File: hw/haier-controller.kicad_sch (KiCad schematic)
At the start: 95 parts, among them J1 USB4105-GF-A, J10 DG240W, J11 DG240W, J12 DG240W, J2 10118194-0001LF, J3 TC2050-IDC-NL, J4 Goldpin, J5 BM04B, J6 S3B-XH-A-1, J7 S3B-XH-A-1, J8 S4B-XH-A-1, J9 S4B-XH-A-1, K1 HFD27-005-S, K2 HFD23/005-1ZS, K3 HFD23/005-1ZS, K4 HFD23/005-1ZS, Q1 MMBT3904, Q2 MMBT3904, Q3 MMBT3904, Q4 MMBT3904, Q5 MMBT3904, SW1 PTS526SM15SMTR2_LFS, U1 ESP32-C6, U2 LM66200DRLR, U3 LD1117S33CTR, U4 USBLC6-4SC6, U5 DS2401+, U6 MAX3485EESA+T

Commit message: Updated R1,R3,J3
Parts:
- J3: footprint (none) -> connectors:TC2050-IDC-NL
- R1, R3: footprint (none) -> SMD:C_0603
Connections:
- no-connect marks 15 -> 16
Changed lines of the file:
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@@
 	)
 	(no_connect
+		(at 182.88 106.68)
+	)
+	(no_connect
 		(at 259.08 121.92)
 	)
@@
 			)
 		)
-		(property "Footprint" ""
+		(property "Footprint" "SMD:C_0603"
 			(at 43.815 40.64 0)
 			(hide yes)
@@
 			)
 		)
-		(property "Footprint" ""
+		(property "Footprint" "SMD:C_0603"
 			(at 43.815 38.1 0)
 			(hide yes)
@@
 			)
 		)
-		(property "Footprint" ""
+		(property "Footprint" "connectors:TC2050-IDC-NL"
 			(at 26.67 137.795 0)
 			(hide yes)

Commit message: Update footprints, Import to PCB
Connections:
- no-connect marks 16 -> 18
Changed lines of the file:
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@@
 	)
 	(no_connect
+		(at 131.445 100.33)
+	)
+	(no_connect
 		(at 41.275 154.305)
 	)
@@
 	)
 	(no_connect
-		(at 182.88 106.68)
+		(at 131.445 102.87)
 	)
 	(no_connect
@@
 	)
 	(no_connect
+		(at 131.445 97.79)
+	)
+	(no_connect
 		(at 196.215 53.975)
 	)
@@
 		(pin "1"
 		)
+		(pin "4"
+		)
 		(instances

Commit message: Finish PCB
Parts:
- removed J3: TC2050-IDC-NL, connectors:TC2050-IDC-NL, symbol Connectors:TC2050-IDC-NL
- added H1, H2, H3, H4: M3, mechanical:M3-Hole, symbol Misc:M3-Mount
- added J3: FTSH-105-01-L-DV-K, connectors:FTSH-105-01-L-DV-K, symbol Connectors:FTSH-105-01-L-DV-K
- R1, R3: footprint SMD:C_0603 -> SMD:R_0603
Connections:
- net 1W_ID: now also U1.14 (IO13); no longer U1.9 (IO1)
- net COOL_SW: now also U1.17 (IO19); no longer U1.11 (IO10)
- net DS18B20: now also U1.13 (IO12); no longer U1.8 (IO0)
- net ESP_EN: now also J3.10 (RST)
- net ESP_TCK: now also J3.4 (TCK/SWDCLK)
- net ESP_TDI: now also U4.4 (I/O3), J3.8 (TDI); no longer U4.6 (I/O4)
- net ESP_TDO: now also U4.6 (I/O4), J3.6 (TDO/SWO); no longer U4.4 (I/O3)
- net ESP_TMS: now also J3.2 (TMS/SWDIO)
- net HEAT_SW: now also U1.18 (IO20); no longer U1.26 (IO3)
- net LIM_SW: now also U1.16 (IO18); no longer U1.12 (IO11)
- net RS_SWITCH: now also U1.12 (IO11); no longer U1.27 (IO2)
- net VBUS: now also C6.2, C7.2, C8.2, D10.1, D11.1, D12.1, D9.1, K1.8 (GND), K2.5 (GND), K3.5 (GND), K4.5 (GND), R2.1, R20.2, R21.2, R22.2, R23.2, TP3.1, U2.2 (VOUT), U2.7 (VOUT), U3.3 (VIN); no longer C1.2, C2.2, J1.A4 (VBUS), J1.A9 (VBUS), TP2.1
- net GND: now reaches Q5.3 (E)
- net GND: now also C1.1, C10.1, C11.1, C12.1, C13.1, C14.1, C15.1, C16.2, C2.1, C3.1, C4.1, C5.1, C6.1, C7.1, C8.1, C9.1, D1.1, D2.1, D3.1, D4.1, D5.1, D6.2, D8.1, J1.A1 (GND), J1.A12 (GND), J1.SH (Shield), J2.5 (GND), J2.SH, J4.2, J5.4, J5.SH, J6.2, J7.2, Q1.3 (E), Q2.3 (E), Q3.3 (E), Q4.3 (E), R1.1, R12.2, R13.2, R3.1, SW1.2, TP6.1, U1.1 (GND), U1.28 (GND), U1.29 (EPAD), U2.1 (GND), U2.4 (~{ON}), U2.5 (GND), U3.1 (GND), U4.2 (GND), U5.1 (GND), U6.5 (GND), H1.1, H2.1, H3.1, H4.1, J3.3 (GND), J3.5 (GND), J3.7 (VDD), J3.9 (GND)
- net +3.3V: now reaches C16.1, U6.8 (VCC)
- net +3.3V: now also C10.2, C11.2, C12.2, C15.2, C9.2, J5.1, J6.3, J7.3, R11.1, R14.1, R4.1, R6.2, R7.1, R8.1, TP4.1, U1.2 (3V3), U3.2 (VOUT), U4.5 (VBUS), J3.1 (VREF)
- net at K4.3 (COM1), K4.4 (COM1): now also J12.2; no longer J12.1
- net at K4.6 (NO1): now also J12.1; no longer J12.2
- net at K2.3 (COM1), K2.4 (COM1): now also J10.2; no longer J10.1
- net at K2.6 (NO1): now also J10.1; no longer J10.2
- net VBUS_B: now reaches C3.2, J2.1 (VCC), TP1.1
- net VBUS_B: now also C4.2, U2.3 (VIN1)
- net VBUS_A: now reaches C5.2, U2.6 (VIN2)
- net VBUS_A: now also C1.2, C2.2, J1.A4 (VBUS), J1.A9 (VBUS), TP2.1
- net at K3.3 (COM1), K3.4 (COM1): now also J11.2; no longer J11.1
- net at K3.6 (NO1): now also J11.1; no longer J11.2
- net at R9.1: now also U1.11 (IO10); no longer U1.16 (IO18)
- no-connect marks 18 -> 19
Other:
- moved on the sheet: J10, J11, J12, J4

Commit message: Clean ERC errors
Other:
- moved on the sheet: C1, C10, C11, C12, C14, C15, C16, C2, C3, C4, C5, C6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

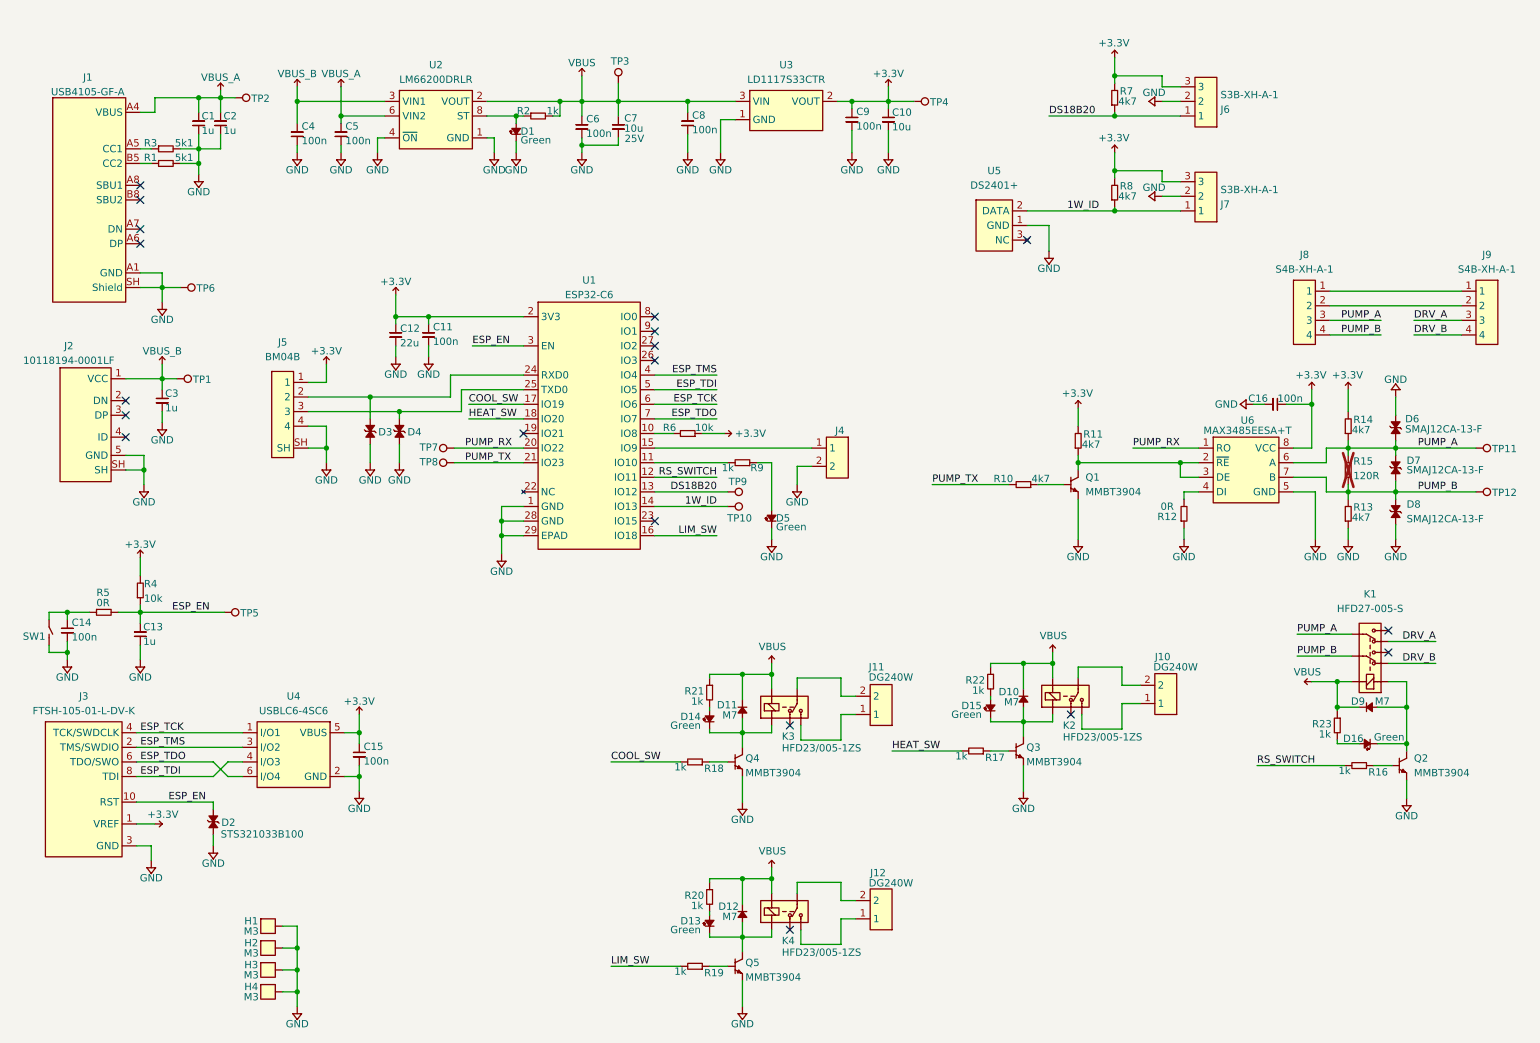
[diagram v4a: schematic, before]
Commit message: Update components, Add silkscreen descriptors
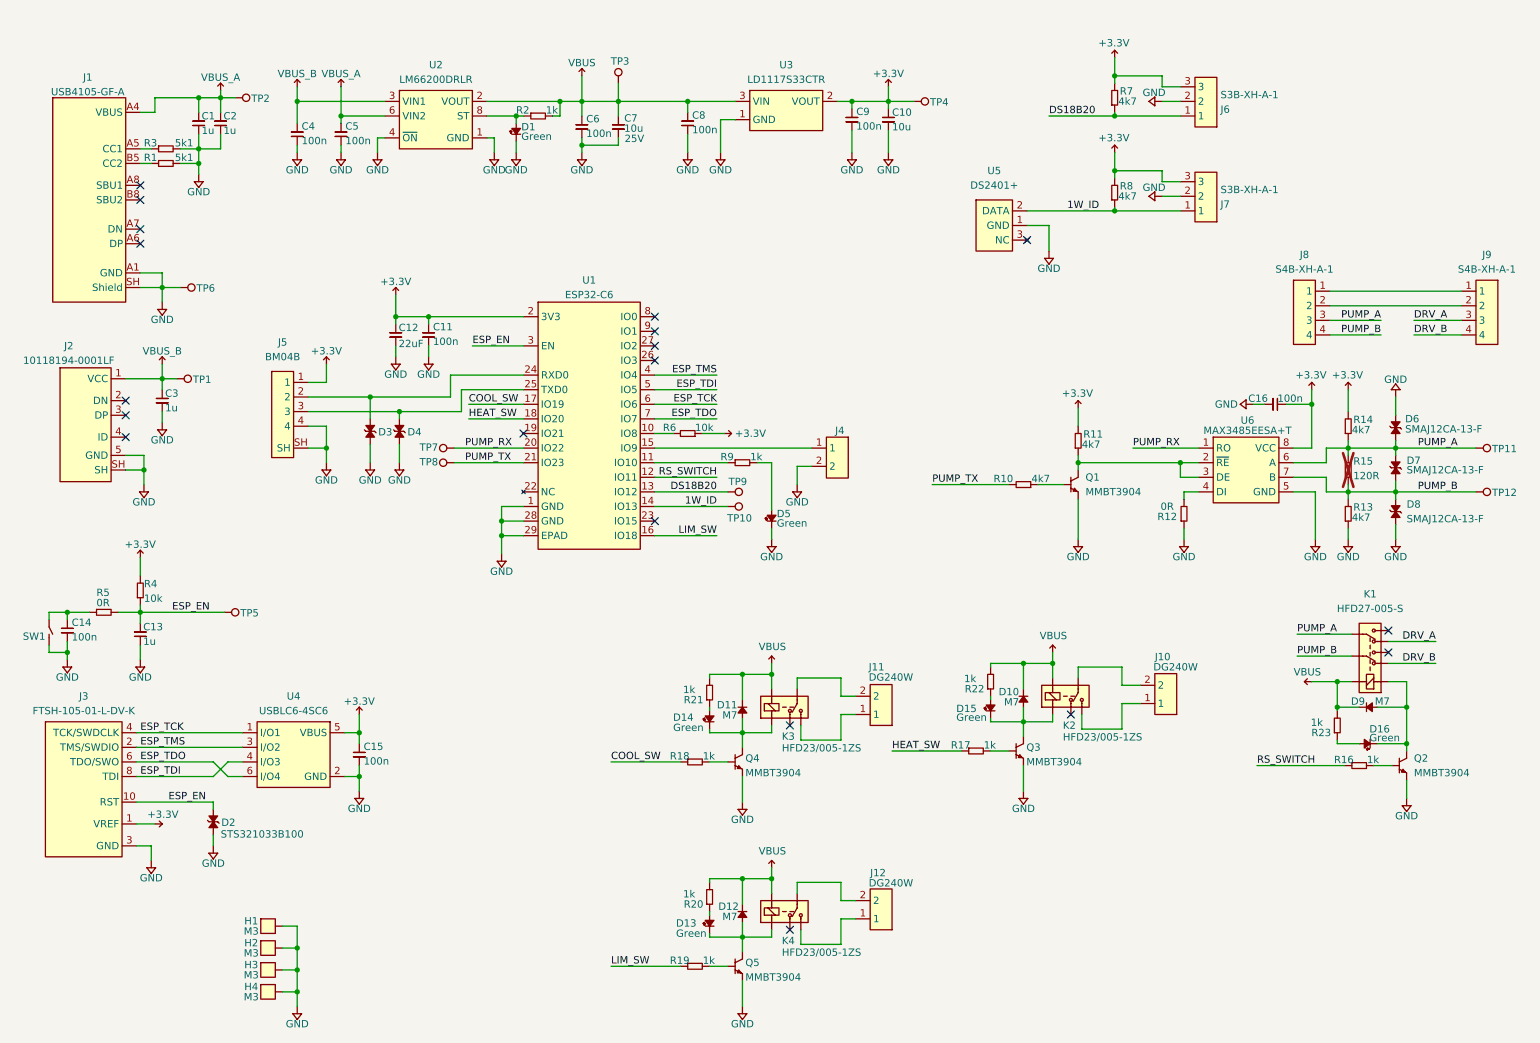
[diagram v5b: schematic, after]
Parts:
- removed C12: 22u, SMD:C_0805, symbol Capacitors:KGM21AR51C226KU
- removed D1, D13, D14, D15, D16, D5: Green, SMD:LED_0603, symbol LEDs:150060VS75000
- removed R16, R17, R18, R19, R2, R20, R21, R22, R23, R9: 1k, SMD:R_0603, symbol Resistors:CRGH0603F1K0
- added C12: 22uF, SMD:C_0805, symbol Capacitors:GRM21BC81C226ME44L
- added D1, D13, D14, D15, D16, D5: Green, SMD:LED_0603, symbol LEDs:LTST-C190KGKT
- added R16, R17, R18, R19, R2, R20, R21, R22, R23, R9: 1k, SMD:R_0603, symbol Resistors:CRCW06031K00FKEA
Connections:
- net +3.3V: now also C12.2
- net COOL_SW: now also R18.2
- net GND: now also C12.1, D1.1, D5.1
- net HEAT_SW: now also R17.2
- net LIM_SW: now also R19.2
- net RS_SWITCH: now also R16.2
- net VBUS: now also R2.1, R20.1, R21.1, R22.1, R23.1
- net at D12.2, K4.2 (VCC), Q5.2 (C): now also D13.1
- net at Q5.1 (B): now also R19.1
- net at Q4.1 (B): now also R18.1
- net at D9.2, K1.1 (VCC), Q2.2 (C): now also D16.1
- net at D11.2, K3.2 (VCC), Q4.2 (C): now also D14.1
- net at D10.2, K2.2 (VCC), Q3.2 (C): now also D15.1
- net at Q2.1 (B): now also R16.1
- net at Q3.1 (B): now also R17.1
- net at U2.8 (ST): now also D1.2, R2.2
- net at U1.11 (IO10): now also R9.2
- new net: D16.2, R23.2
- new net: D5.2, R9.1
- new net: D14.2, R21.2
- new net: D13.2, R20.2
- new net: D15.2, R22.2

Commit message: Add Pull down resistors, Change USB micro to DNP, Change ROM to DNP
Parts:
- added R24, R25, R26, R27: 10k, SMD:R_0603, symbol Resistors:CRGH0603F10K
- added R28, R29: 0R, SMD:R_0603, symbol Resistors:CRCW06030000Z0EI
- C3, C4, D1, J2, J7, R2, R8, U2, U5: now not fitted
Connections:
- net COOL_SW: now also R25.2
- net GND: now also R24.1, R25.1, R26.1, R27.1
- net HEAT_SW: now also R26.2
- net LIM_SW: now also R24.2
- net RS_SWITCH: now also R27.2
- net VBUS: now also R28.1, R29.1
- net VBUS_A: now also R28.2
- net VBUS_B: now also R29.2
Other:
- company: (none) -> MRWorkshop
- title: (none) -> Haier Controller
